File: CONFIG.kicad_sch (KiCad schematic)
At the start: 23 parts, among them IC1 ECP5-BGA256, J1 Conn_01x07, U5 AT25SF081-SSHD-X

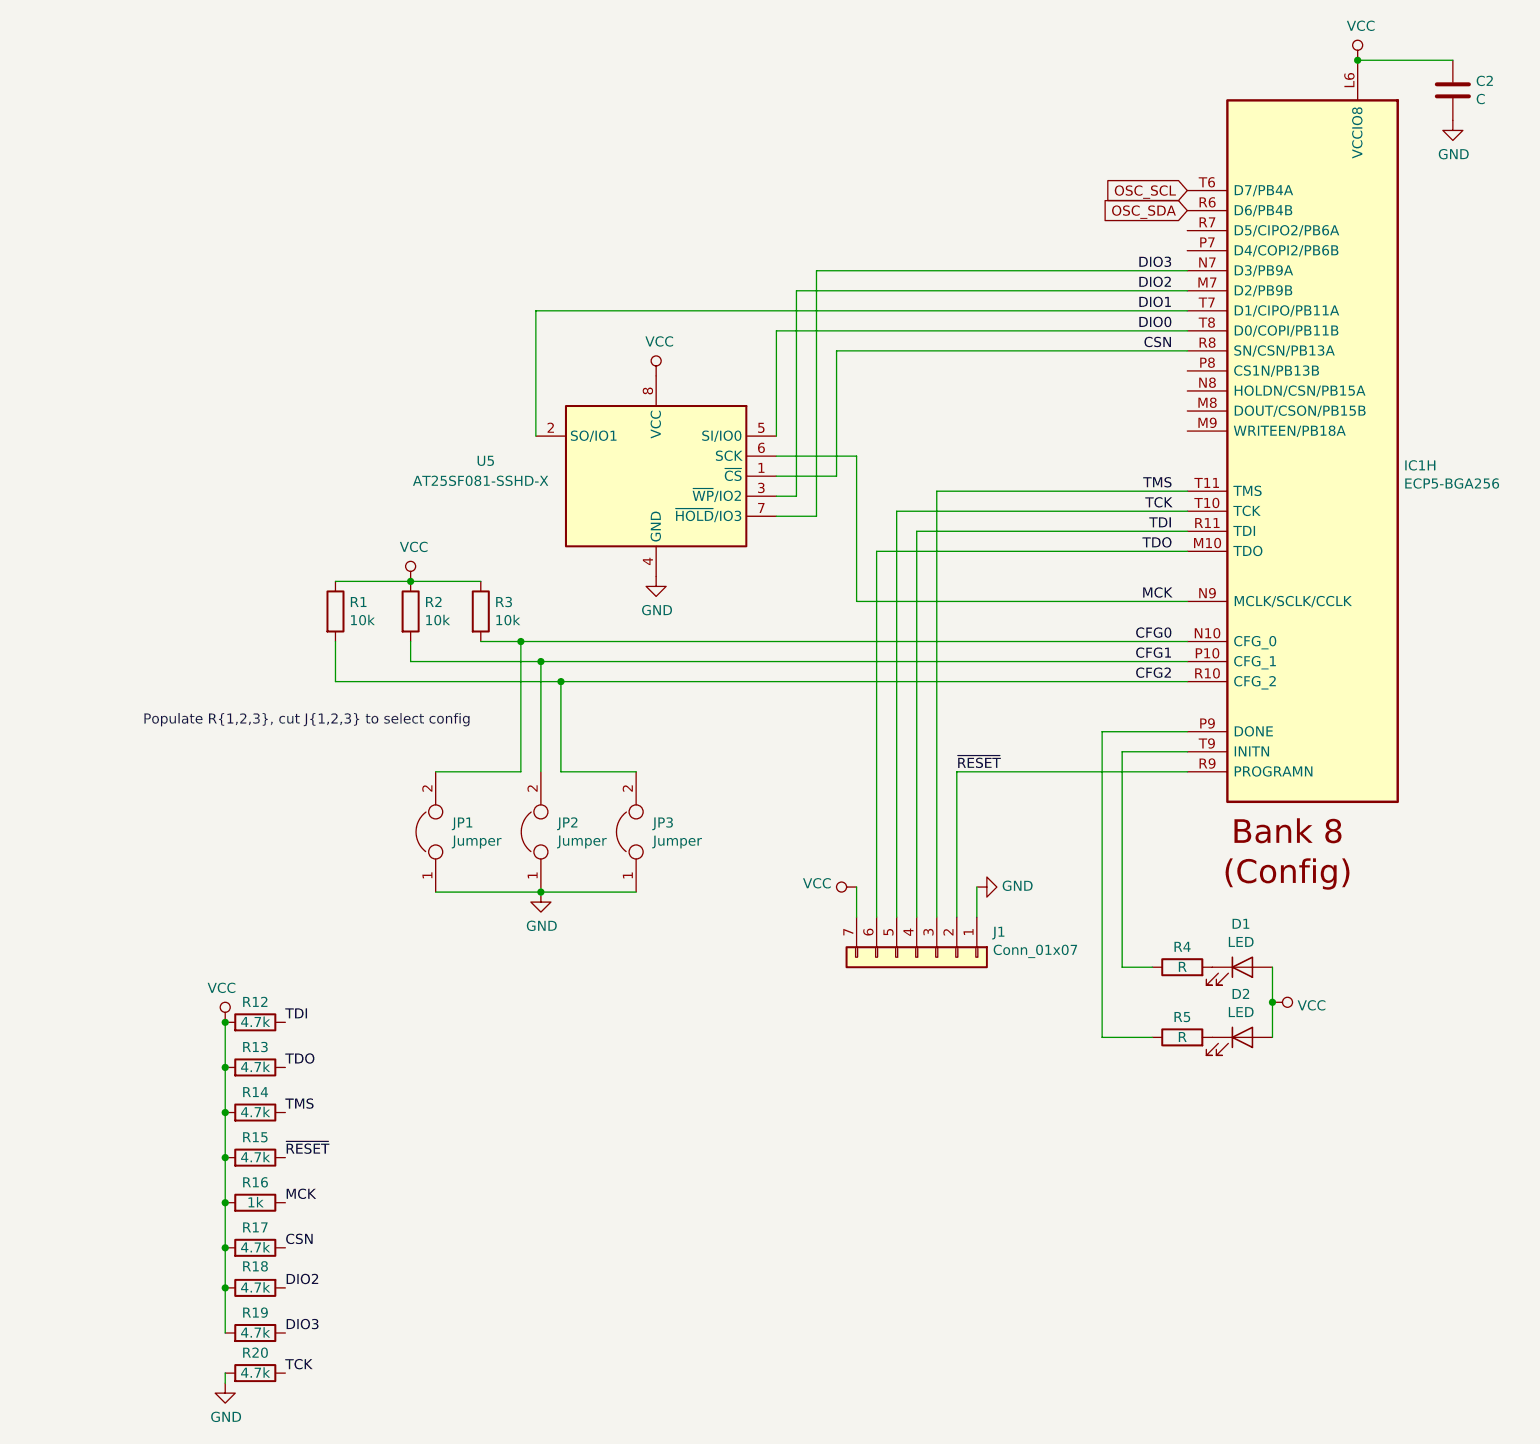
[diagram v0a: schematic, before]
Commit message: Remove SD card, relocate regulators
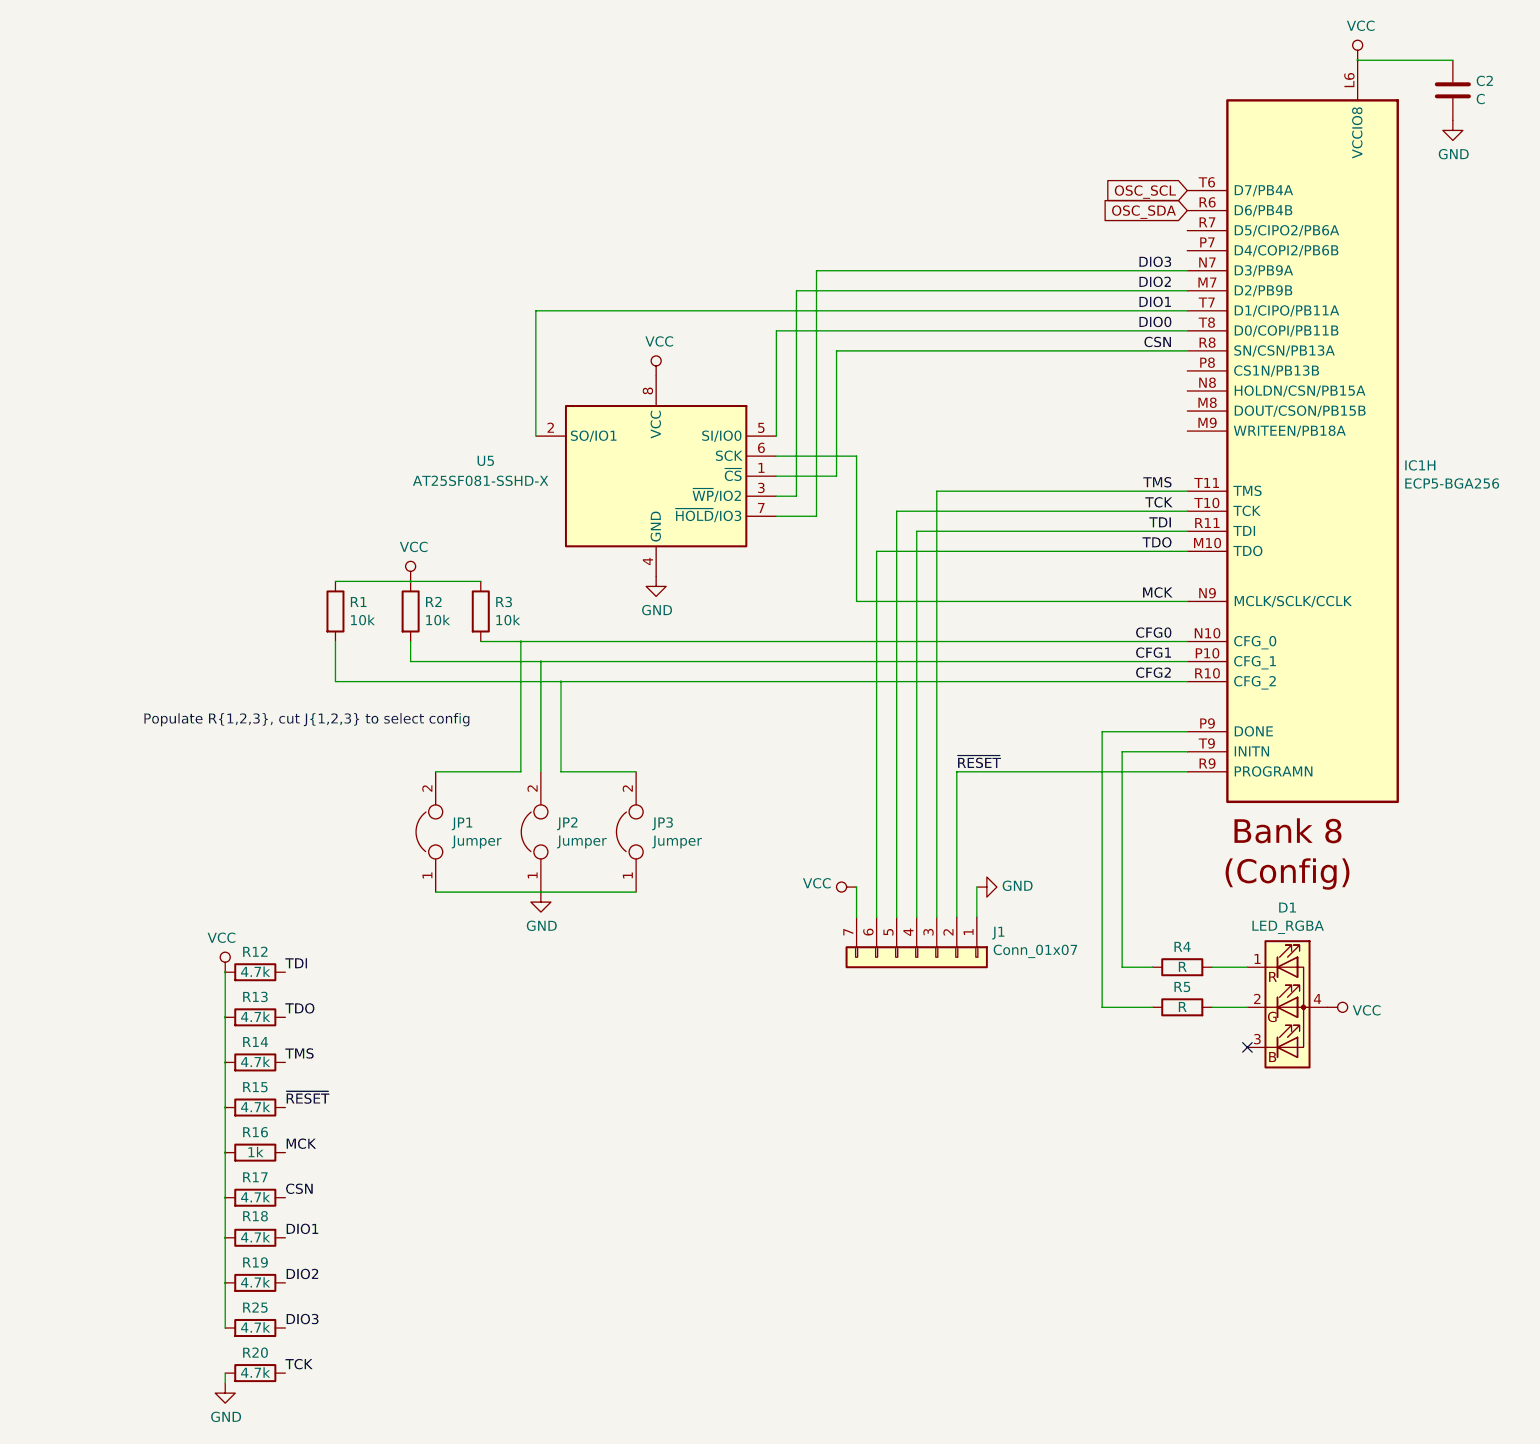
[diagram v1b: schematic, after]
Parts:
- removed D1, D2: LED, LED_SMD:LED_0805_2012Metric_Castellated, symbol Device:LED
- added D1: LED_RGBA, mini-mipi:LED_0404, symbol Device:LED_RGBA
- added R25: 4.7k, Resistor_SMD:R_0402_1005Metric, symbol Device:R
- U5: footprint Package_SO:SOIC-8_3.9x4.9mm_P1.27mm -> Package_SO:SOIC-8_5.275x5.275mm_P1.27mm
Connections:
- net DIO1: now also R18.2
- net DIO2: now also R19.1; no longer R18.2
- net DIO3: now also R25.1; no longer R19.1
- net VCC: now also D1.4 (A), R25.2
- net at R5.2: now also D1.2 (GK)
- net at R4.2: now also D1.1 (RK)
- no-connect marks 0 -> 1
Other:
- moved on the sheet: R12, R13, R14, R15, R16, R17, R18, R19, R5

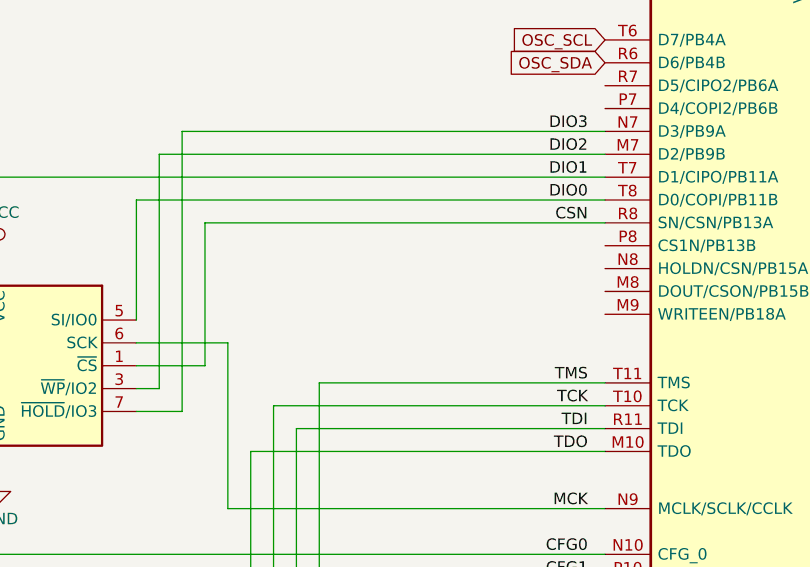
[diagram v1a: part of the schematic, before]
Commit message: Fix incorrect flash CSN pin
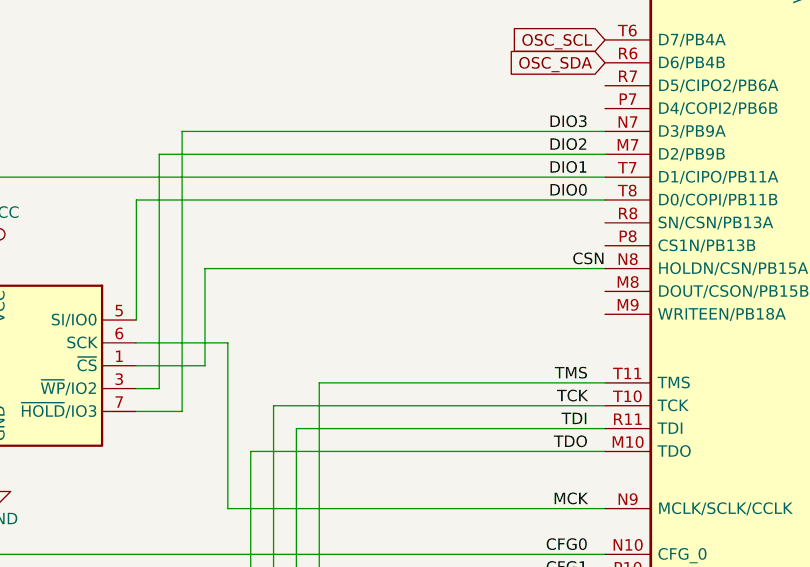
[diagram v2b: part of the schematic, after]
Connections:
- net CSN: now also IC1.N8 (HOLDN/CSN/PB15A); no longer IC1.R8 (SN/CSN/PB13A)
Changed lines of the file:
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@@
-(kicad_sch (version 20200714) (host eeschema "5.99.0-unknown-027b6c8cf~102~ubuntu20.04.1")
+(kicad_sch (version 20200820) (host eeschema "5.99.0-unknown-35eda030a~103~ubuntu20.04.1")
   (page 4 6)
   (paper "A4")
@@
     (stroke (width 0) (type solid) (color 0 0 0 0))
   )
-  (wire (pts (xy 170.18 55.88) (xy 170.18 71.755))
-    (stroke (width 0) (type solid) (color 0 0 0 0))
-  )
-  (wire (pts (xy 170.18 55.88) (xy 214.63 55.88))
+  (wire (pts (xy 170.18 60.96) (xy 170.18 71.755))
+    (stroke (width 0) (type solid) (color 0 0 0 0))
+  )
+  (wire (pts (xy 170.18 60.96) (xy 214.63 60.96))
     (stroke (width 0) (type solid) (color 0 0 0 0))
   )
@@
     (effects (font (size 1.27 1.27)) (justify right bottom))
   )
-  (label "CSN" (at 212.725 55.88 180)
-    (effects (font (size 1.27 1.27)) (justify right bottom))
-  )
   (label "TMS" (at 212.725 73.66 180)
     (effects (font (size 1.27 1.27)) (justify right bottom))
@@
     (effects (font (size 1.27 1.27)) (justify right bottom))
   )
+  (label "CSN" (at 214.63 60.96 180)
+    (effects (font (size 1.27 1.27)) (justify right bottom))
+  )
